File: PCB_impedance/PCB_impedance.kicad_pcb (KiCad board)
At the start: 4 copper layers, 65 x 56 mm, 50 parts, among them J2 Conn_02x20_Odd_Even, J6 Conn_01x16_Socket, U1 ADG726BSUZ, U2 ADG726BSUZ, U3 ADG726BSUZ, U5 ADG726BSUZ, U6 AD5941, U7 MCP1727-3302xMF

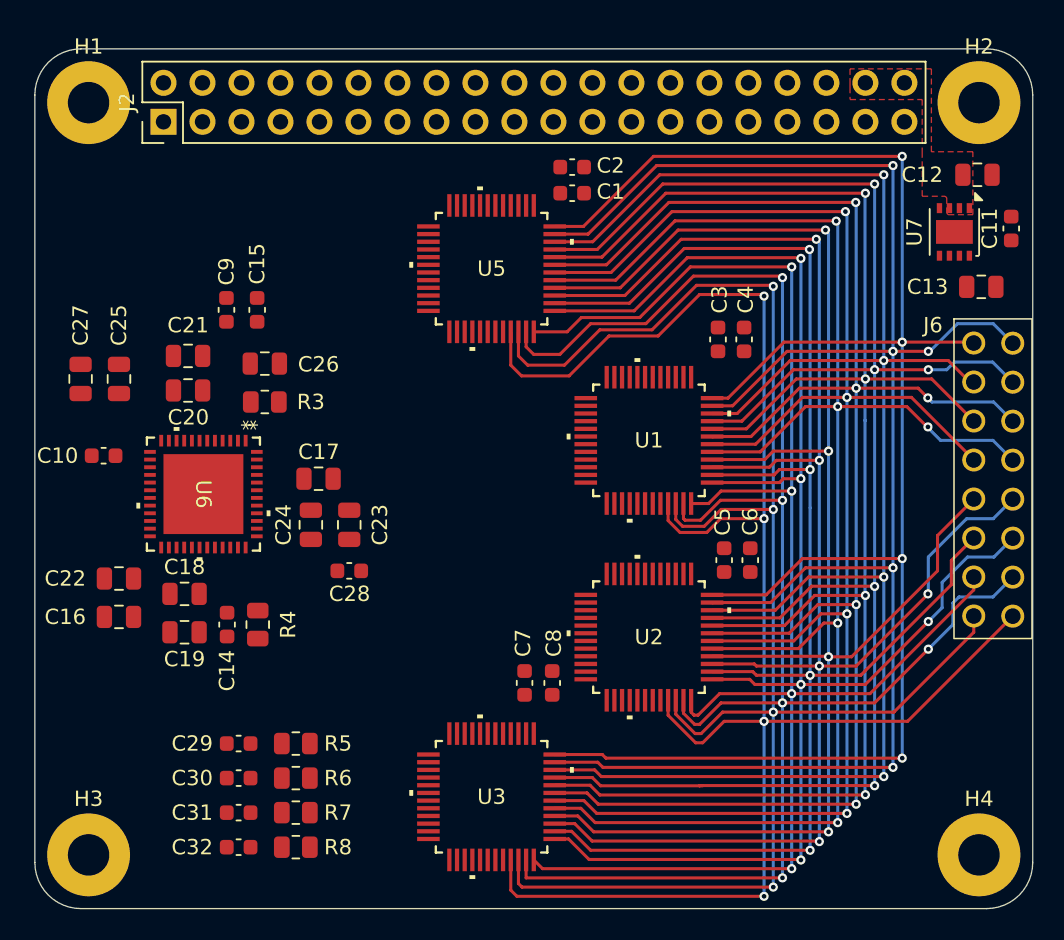
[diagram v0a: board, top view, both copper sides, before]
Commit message: PCB routing with the AD5940 is complete
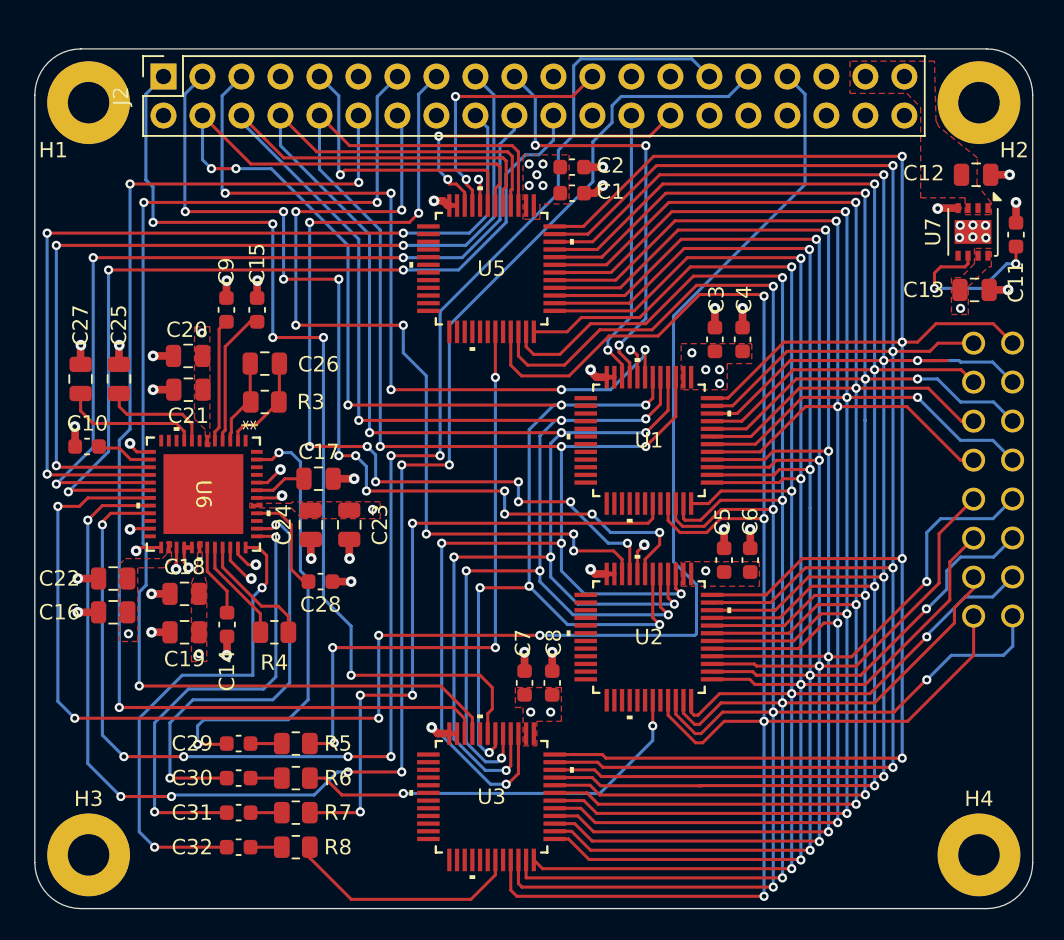
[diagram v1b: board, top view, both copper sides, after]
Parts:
- J2: footprint lib_mesure_impedance:PinHeader_2x20_P2.54mm_Vertical -> Connector_PinSocket_2.54mm:PinSocket_2x20_P2.54mm_Vertical
- J6: moved to B.Cu
- moved J6 5.11 mm to (119.5, 84.1), turned to 180 degrees
- moved J2 2.95 mm to (62.9, 68.3)
- moved C20 2.25 mm to (64.5, 86.5)
- moved C21 2.20 mm to (64.5, 88.7)
- moved C28 2.01 mm to (73.1, 101.2)
- moved C10 1.24 mm to (57.9, 92.4)
- moved U7 1.21 mm to (115.6, 78.4)
- moved R4 1.19 mm to (70.1, 104.5), turned to 0 degrees
- moved C11 0.51 mm to (118.4, 78.6)
- moved C16 0.48 mm to (59.6, 103.2)
- moved C13 0.48 mm to (115.7, 82.2)
- moved C22 0.38 mm to (59.6, 101.0)
- moved C3 0.20 mm to (98.8, 85.4)
- moved C4 0.10 mm to (100.6, 85.4)
- moved C12 0.09 mm to (115.8, 74.7)
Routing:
- net /MUX_A3: track 0.00 -> 111.7 mm, vias 0 -> 9
- net /MUX_A0: track 0.00 -> 110.8 mm, vias 0 -> 7
- net /MUX_A2: track 0.00 -> 110.3 mm, vias 0 -> 7
- net /MUX_A1: track 0.00 -> 110.3 mm, vias 0 -> 7
- net /GPIO0_INT_AD: track 0.00 -> 107.4 mm, vias 0 -> 5
- net /GPIO1_AD: track 0.00 -> 102.9 mm, vias 0 -> 7
- net /GPIO2_AD: track 0.00 -> 97.9 mm, vias 0 -> 7
- net /MUX_WR3: track 0.00 -> 79.3 mm, vias 0 -> 3
- net /MUX_EN3: track 0.00 -> 77.5 mm, vias 0 -> 3
- net /MUX_CSA3: track 0.00 -> 64.1 mm, vias 0 -> 5
- net /MUX_CSA2: track 0.00 -> 63.3 mm, vias 0 -> 11
- net /CEn_SPI0_AD: track 0.00 -> 59.4 mm, vias 0 -> 3
- net /MUX_WR2: track 0.00 -> 58.8 mm, vias 0 -> 9
- net GND: track 0.00 -> 58.5 mm, vias 0 -> 47
- net /SCLK_AD: track 0.00 -> 58.4 mm, vias 0 -> 3
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- added copper zone on F.Cu, net +3V3
